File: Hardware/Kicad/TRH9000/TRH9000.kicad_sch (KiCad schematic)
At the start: 6 parts, among them J1 MSX_SLOT_CONNECTOR, U4 74HC138, U5 74HC32

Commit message: Footprint for the V9990
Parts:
- U4: footprint (none) -> Package_SO:SO-16_3.9x9.9mm_P1.27mm
- U5: footprint digikey-footprints:DIP-14_W3mm -> Package_SO:SO-14_3.9x8.65mm_P1.27mm
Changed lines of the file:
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@@
       (effects (font (size 1.27 1.27)) (justify left))
     )
-    (property "Footprint" "digikey-footprints:DIP-14_W3mm" (id 2) (at 165.1 120.65 0)
+    (property "Footprint" "Package_SO:SO-14_3.9x8.65mm_P1.27mm" (id 2) (at 165.1 120.65 0)
       (effects (font (size 1.524 1.524)) (justify left) hide)
     )
@@
       (effects (font (size 1.27 1.27)) (justify left))
     )
-    (property "Footprint" "" (id 2) (at 118.11 128.27 0)
+    (property "Footprint" "Package_SO:SO-16_3.9x9.9mm_P1.27mm" (id 2) (at 118.11 128.27 0)
       (effects (font (size 1.27 1.27)) hide)
     )
@@
     )
     (path "/d5c7e94e-ee8c-4fa2-b6f9-333fadc34caa/da6bfb64-a33a-4cf2-a14f-42ddd8c8c720"
-      (reference "C2") (unit 1) (value "100nF") (footprint "")
+      (reference "C2") (unit 1) (value "100nF") (footprint "Capacitor_SMD:C_0805_2012Metric")
     )
     (path "/d5c7e94e-ee8c-4fa2-b6f9-333fadc34caa/7abbb0b8-25fa-4ba9-afed-652280d66707"
@@
       (reference "R6") (unit 1) (value "4K7") (footprint "LED_SMD:LED_0805_2012Metric")
     )
-    (path "/d9ed34ef-ff83-4a70-a9f7-db0f42d1292e/67662d22-a245-4940-bd65-03651bcaa81c"
-      (reference "R7") (unit 1) (value "470R") (footprint "LED_SMD:LED_0805_2012Metric")
-    )
     (path "/d9ed34ef-ff83-4a70-a9f7-db0f42d1292e/bbaafd10-2e61-4d37-80f8-27fc5a2b4449"
       (reference "R8") (unit 1) (value "2K2") (footprint "LED_SMD:LED_0805_2012Metric")
     )
-    (path "/d9ed34ef-ff83-4a70-a9f7-db0f42d1292e/37410a4d-2046-4ddf-bb0e-18d481708b5d"
-      (reference "R9") (unit 1) (value "470R") (footprint "LED_SMD:LED_0805_2012Metric")
-    )
-    (path "/d9ed34ef-ff83-4a70-a9f7-db0f42d1292e/643d4177-75b8-41e9-8c82-b89d4a4fad42"
-      (reference "R10") (unit 1) (value "470R") (footprint "LED_SMD:LED_0805_2012Metric")
-    )
     (path "/d9ed34ef-ff83-4a70-a9f7-db0f42d1292e/fc1eeac4-dcc2-422b-a258-9423bfa5a1ef"
       (reference "R11") (unit 1) (value "4K7") (footprint "LED_SMD:LED_0805_2012Metric")
@@
       (reference "R23") (unit 1) (value "240R") (footprint "LED_SMD:LED_0805_2012Metric")
     )
+    (path "/d9ed34ef-ff83-4a70-a9f7-db0f42d1292e/ca541a19-f6cc-45bc-af9b-19d34164bfc7"
+      (reference "RV1") (unit 1) (value "500R") (footprint "Potentiometer_SMD:Potentiometer_Bourns_3314G_Vertical")
+    )
+    (path "/d9ed34ef-ff83-4a70-a9f7-db0f42d1292e/1325e162-b47f-49fb-8630-ad924a927842"
+      (reference "RV2") (unit 1) (value "500R") (footprint "Potentiometer_SMD:Potentiometer_Bourns_3314G_Vertical")
+    )
+    (path "/d9ed34ef-ff83-4a70-a9f7-db0f42d1292e/a3e1189c-b975-4c18-acc9-478a0dd0a5b4"
+      (reference "RV3") (unit 1) (value "500R") (footprint "Potentiometer_SMD:Potentiometer_Bourns_3314G_Vertical")
+    )
     (path "/d5c7e94e-ee8c-4fa2-b6f9-333fadc34caa/c04f413f-eb21-4d40-8e64-40127e6da87a"
-      (reference "U1") (unit 1) (value "V9990") (footprint "Ddraig:QFP-128_28x28_Pitch0.8mm")
+      (reference "U1") (unit 1) (value "V9990") (footprint "trh9000:QFP-128_28x28_Pitch0.8mm")
     )
     (path "/d5c7e94e-ee8c-4fa2-b6f9-333fadc34caa/957e464e-fa1e-4fdd-98f3-d28c0b05174e"
@@
     )
     (path "/f2de766b-6e04-4297-9ac6-8ed19da3519b"
-      (reference "U4") (unit 1) (value "74HC138") (footprint "")
+      (reference "U4") (unit 1) (value "74HC138") (footprint "Package_SO:SO-16_3.9x9.9mm_P1.27mm")
     )
     (path "/2c31a37b-5a2e-4dde-9eb0-70323652ba66"
-      (reference "U5") (unit 1) (value "74HC32") (footprint "digikey-footprints:DIP-14_W3mm")
+      (reference "U5") (unit 1) (value "74HC32") (footprint "Package_SO:SO-14_3.9x8.65mm_P1.27mm")
     )
     (path "/d9ed34ef-ff83-4a70-a9f7-db0f42d1292e/a944b42d-633e-4624-b6a6-e9241b129cf1"

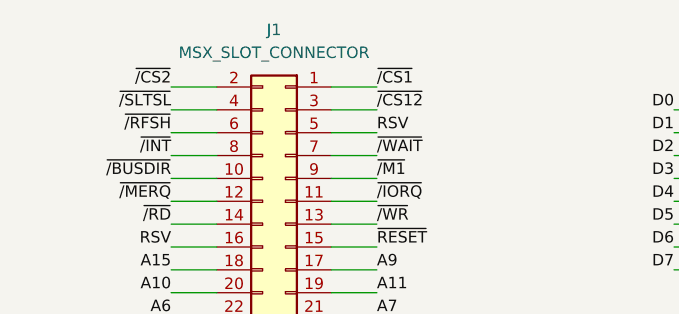
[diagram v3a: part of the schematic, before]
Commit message: Footprint adjusts
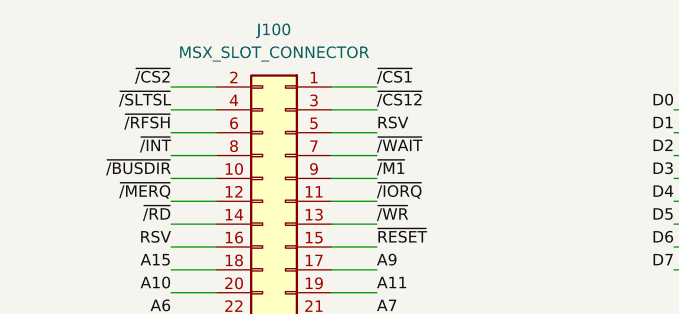
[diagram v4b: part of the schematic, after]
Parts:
- J100: renamed from J1; now left out of the parts list
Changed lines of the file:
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@@
   )
   (symbol (lib_id "Connector_Generic:Conn_02x25_Odd_Even") (at 48.26 55.88 0) (mirror y) (unit 1)
-    (in_bom yes) (on_board yes) (fields_autoplaced)
-    (property "Reference" "J1" (id 0) (at 46.99 19.05 0))
+    (in_bom no) (on_board yes) (fields_autoplaced)
+    (property "Reference" "J100" (id 0) (at 46.99 19.05 0))
     (property "Value" "MSX_SLOT_CONNECTOR" (id 1) (at 46.99 21.59 0))
     (property "Footprint" "msx:msx_cartridge" (id 2) (at 48.26 55.88 0)
@@
       (reference "C24") (unit 1) (value "220uF") (footprint "Capacitor_THT:CP_Radial_D5.0mm_P2.50mm")
     )
-    (path "/5c1dc888-6f7a-4cd6-bda7-5a87c57e6ccc"
-      (reference "J1") (unit 1) (value "MSX_SLOT_CONNECTOR") (footprint "msx:msx_cartridge")
+    (path "/d9ed34ef-ff83-4a70-a9f7-db0f42d1292e/c01ad78a-8b71-4615-ba6a-b588562a7eff"
+      (reference "J1") (unit 1) (value "RGB") (footprint "Connector_Dsub:DSUB-15-HD_Female_Horizontal_P2.29x1.98mm_EdgePinOffset3.03mm_Housed_MountingHolesOffset4.94mm")
     )
     (path "/d9ed34ef-ff83-4a70-a9f7-db0f42d1292e/8a9fe807-e426-499b-ab72-b66db1aca921"
@@
       (reference "J3") (unit 1) (value "Composite") (footprint "trh9000:KLPX0848A2RG")
     )
-    (path "/d9ed34ef-ff83-4a70-a9f7-db0f42d1292e/c01ad78a-8b71-4615-ba6a-b588562a7eff"
-      (reference "J4") (unit 1) (value "DB15_Female_HighDensity") (footprint "Connector_Dsub:DSUB-15-HD_Female_Horizontal_P2.29x1.98mm_EdgePinOffset3.03mm_Housed_MountingHolesOffset4.94mm")
+    (path "/5c1dc888-6f7a-4cd6-bda7-5a87c57e6ccc"
+      (reference "J100") (unit 1) (value "MSX_SLOT_CONNECTOR") (footprint "msx:msx_cartridge")
     )
     (path "/d5c7e94e-ee8c-4fa2-b6f9-333fadc34caa/ed13ecf5-0a7e-4a18-a92b-e7a01e79ff05"

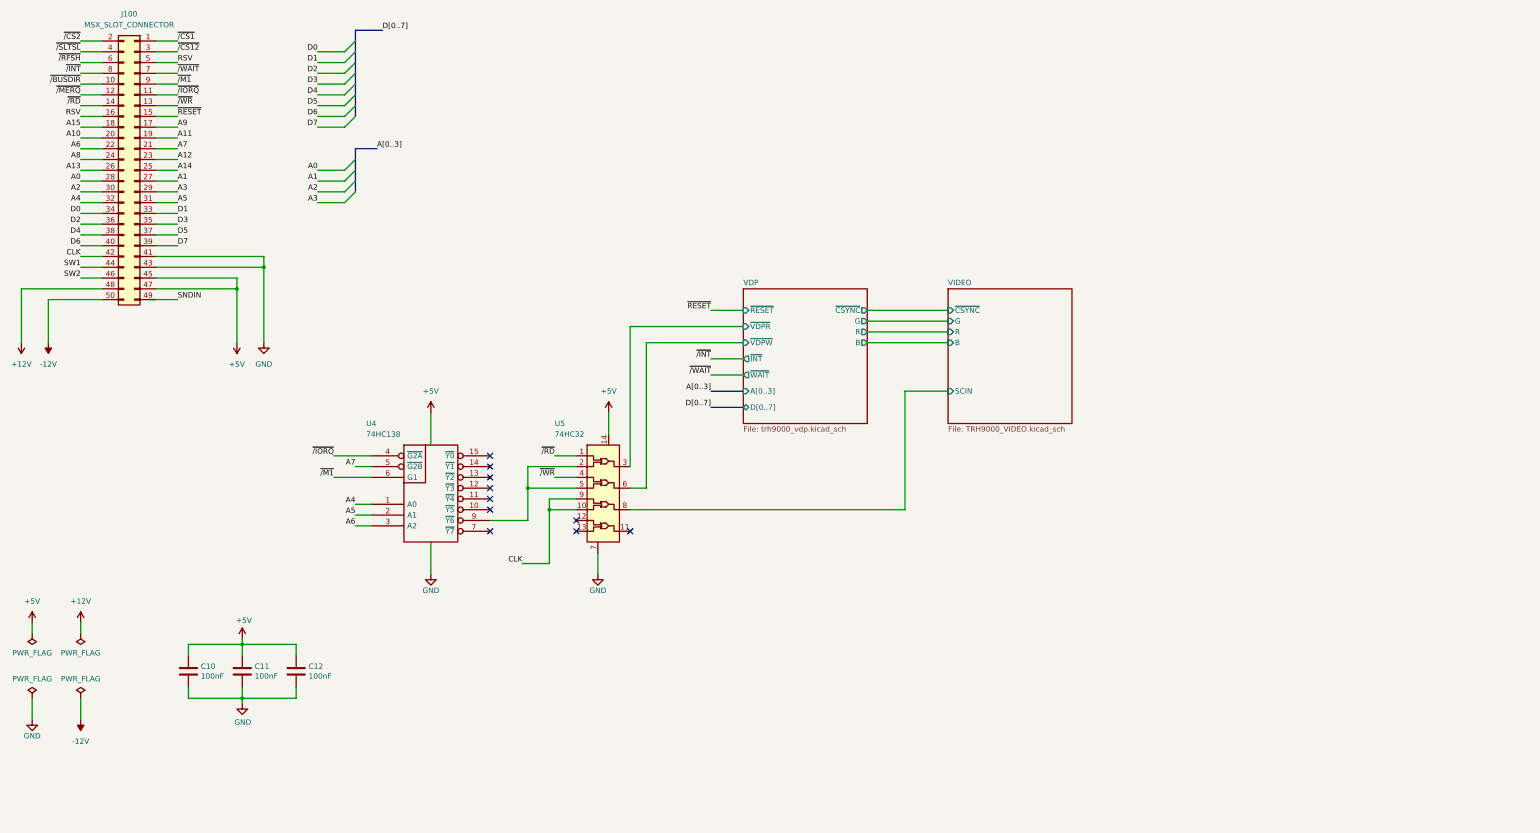
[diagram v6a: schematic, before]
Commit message: Many changes, among them, replacing the Composite out with SCART-rgb.
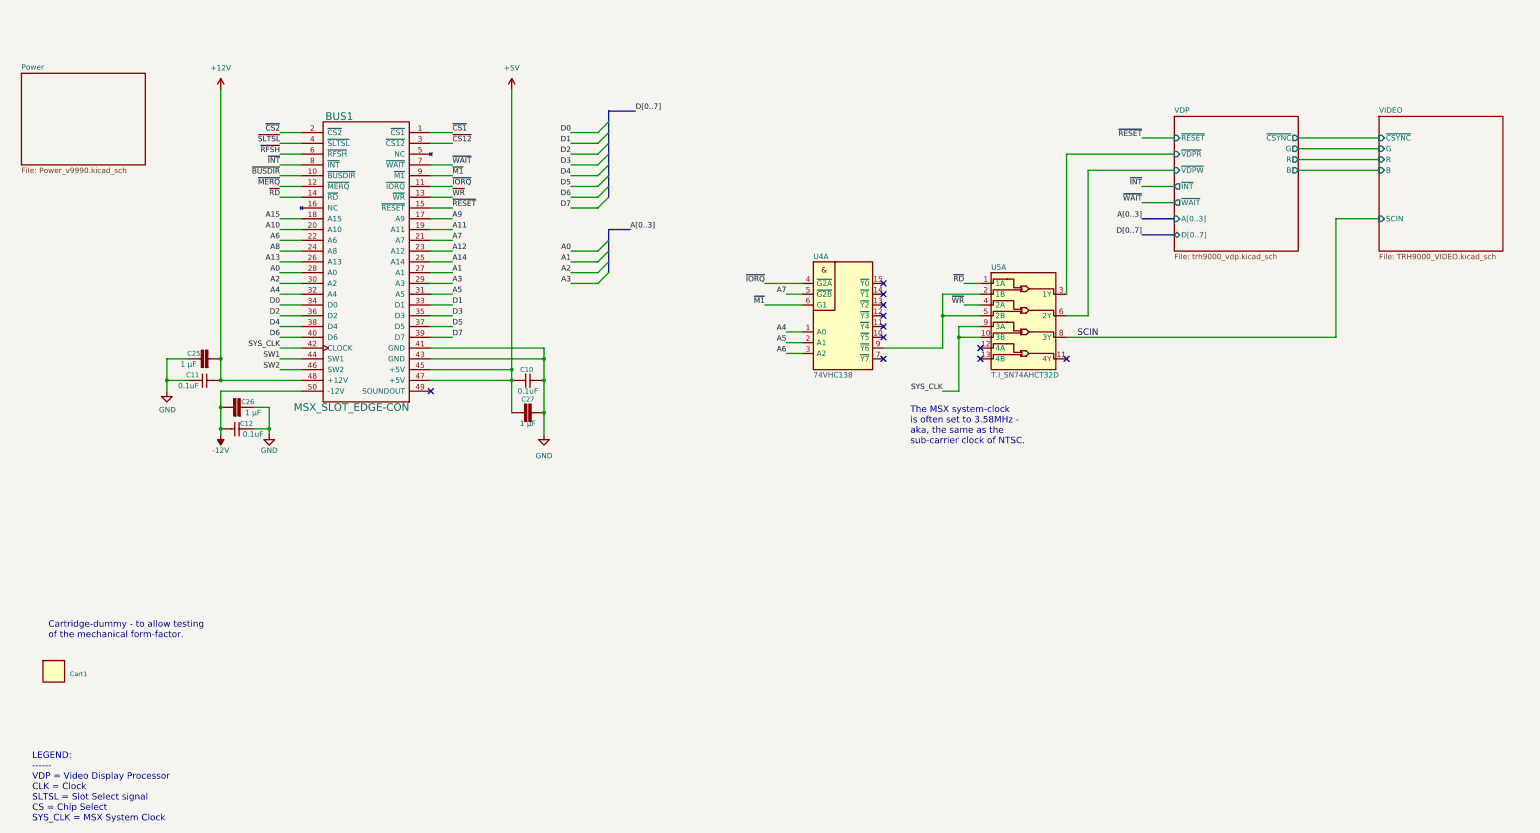
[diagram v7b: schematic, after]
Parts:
- removed C10, C11, C12: 100nF, Capacitor_SMD:C_0805_2012Metric, symbol Device:C
- removed J100: MSX_SLOT_CONNECTOR, msx:msx_cartridge, symbol Connector_Generic:Conn_02x25_Odd_Even
- added BUS1: MSX_SLOT_EDGE-CON, trh9000:msx_cartridge, symbol TRH9000:MSX_SLOT_EDGE-CON
- added C10, C11, C12: C_CC0805JPX7R9BB104, Capacitor_SMD:C_0805_2012Metric, symbol LRJ-parts:C_CC0805JPX7R9BB104
- added C25, C26, C27: C_CL21B105KBFNNNF, Capacitor_SMD:C_0805_2012Metric_Pad1.18x1.45mm_HandSolder, symbol LRJ-parts:C_CL21B105KBFNNNF
- added Cart1: MSX-cartridge_dummy, trh9000:MSX-cart-dummy, symbol TRH9000:MSX-cartridge_dummy
- U4: value 74HC138 -> 74VHC138; symbol 74xx_IEEE:74LS138 -> TRH9000:74VHC138; MPN (none) -> 74VHC138FT; Manufacturer (none) -> Toshiba Semiconductor and Storage
- U5: value 74HC32 -> T.I_SN74AHCT32D; footprint Package_SO:SO-14_3.9x8.65mm_P1.27mm -> trh9000:Texas_R-PDSO-G14_3.6x4.4mm; symbol dk_Logic-Gates-and-Inverters:SN74HC32N -> TRH9000:T.I_SN74AHCT32D; Category Integrated Circuits (ICs) -> (none); DK_Datasheet_Link http://www.ti.com/general/docs/suppproductinfo.tsp?distId=1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 -> (none); DK_Detail_Page /product-detail/en/texas-instruments/SN74HC32N/296-1589-5-N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 -> https://www.digikey.se/en/products/detail/texas-instruments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; Digi-Key_PN 296-1589-5-ND -> (none); Family Logic - Gates and Inverters -> (none); MPN SN74HC32N -> SN74AHCT32DGVR
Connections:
- net +12V: now also BUS1.48 (+12V), C11.2, C25.2
- net +5V: now also BUS1.45 (+5V), BUS1.47 (+5V), C10.1, C27.1; no longer U4.16 (VCC), U5.14 (VCC)
- net -12V: now also BUS1.50 (-12V), C12.1, C26.1
- net A0: now also BUS1.28 (A0)
- net A1: now also BUS1.27 (A1)
- net A10: now also BUS1.20 (A10)
- net A11: now also BUS1.19 (A11)
- net A12: now also BUS1.23 (A12)
- net A13: now also BUS1.26 (A13)
- net A14: now also BUS1.25 (A14)
- net A15: now also BUS1.18 (A15)
- net A2: now also BUS1.30 (A2)
- net A3: now also BUS1.29 (A3)
- net A4: now also BUS1.32 (A4)
- net A5: now also BUS1.31 (A5)
- net A6: now also BUS1.22 (A6)
- net A7: now also BUS1.21 (A7)
- net A8: now also BUS1.24 (A8)
- net A9: now also BUS1.17 (A9)
- net D0: now also BUS1.34 (D0)
- net D1: now also BUS1.33 (D1)
- net D2: now also BUS1.36 (D2~{})
- net D3: now also BUS1.35 (D3)
- net D4: now also BUS1.38 (D4)
- net D5: now also BUS1.37 (D5)
- net D6: now also BUS1.40 (D6)
- net D7: now also BUS1.39 (D7)
- net GND: now also BUS1.41 (GND), BUS1.43 (GND), C10.2, C11.1, C12.2, C25.1, C26.2, C27.2; no longer U4.8 (GND), U5.7 (GND)
- net SW1: now also BUS1.44 (SW1)
- net SW2: now also BUS1.46 (SW2)
- net ~{RESET}: now also BUS1.15 (~{RESET})
- net CLK renamed SYS_CLK
- net SYS_CLK: now also BUS1.42 (CLOCK)
- net VIDEO/SCIN renamed SCIN
- net ~{/IORQ} renamed ~{IORQ}
- net ~{IORQ}: now also BUS1.11 (~{IORQ})
- net ~{/M1} renamed ~{M1}
- net ~{M1}: now also BUS1.9 (~{M1})
- net ~{/RD} renamed ~{RD}
- net ~{RD}: now also BUS1.14 (~{RD})
- net ~{/WR} renamed ~{WR}
- net ~{WR}: now also BUS1.13 (~{WR})
- new net ~{BUSDIR}: BUS1.10 (~{BUSDIR})
- new net ~{CS12}: BUS1.3 (~{CS12})
- new net ~{CS1}: BUS1.1 (~{CS1})
- new net ~{CS2}: BUS1.2 (~{CS2})
- new net ~{INT}: BUS1.8 (~{INT})
- new net ~{MERQ}: BUS1.12 (~{MERQ})
- new net ~{RFSH}: BUS1.6 (~{RFSH})
- new net ~{SLTSL}: BUS1.4 (~{SLTSL})
- new net ~{WAIT}: BUS1.7 (~{WAIT})
- no-connect marks 10 -> 11
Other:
- added sheet Power (Power_v9990.kicad_sch)
- note added: "Cartridge-dummy - to allow testing of the mechanical form-factor."
- note added: "LEGEND: ------ VDP = Video Display Processor CLK = Clock SLTSL = Slot Select signal CS = Chip Select SYS_CLK = MSX System Clock"
- note added: "The MSX system-clock is often set to 3.58MHz - aka, the same as the sub-carrier clock of NTSC."

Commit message: Multiple updates. Routing. Almost finished routing for the VDP. Moved back the footprint for the 14mhz oscillator to THT as it is easier to find outside US/Europe and I have a bunch laying around here. Organized all components into the PCB. Removed the holed in the cartridge so I can better measure them in the standard MSX cartridge. Changed the RGB connector footprint to a shorter version so we can fit it in the standard size cartridge. Fixed multiple footprints to 0805 as we will be standardizing in that size.
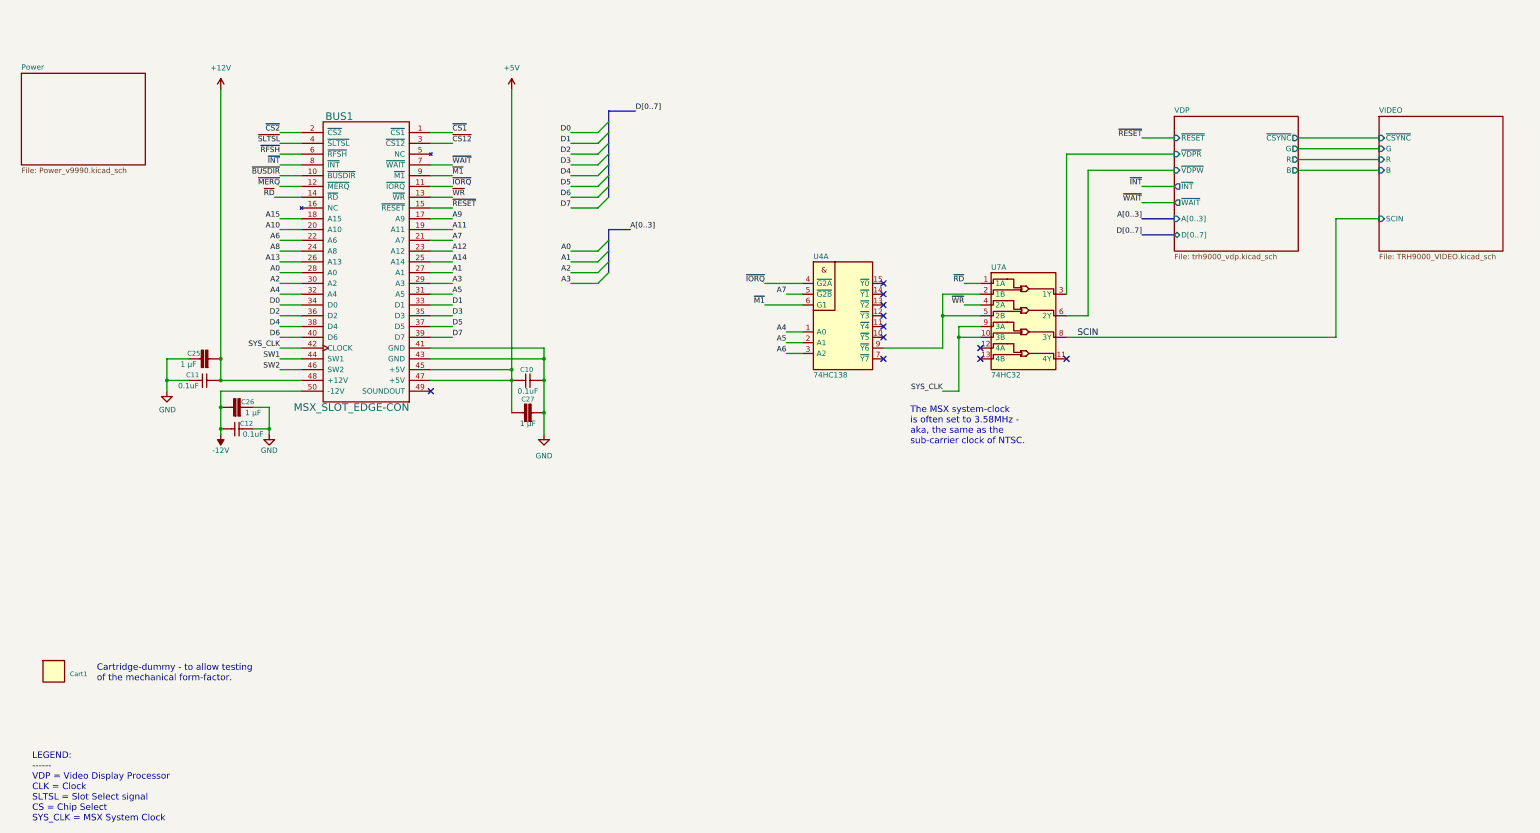
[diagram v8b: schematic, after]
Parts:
- C10: value C_CC0805JPX7R9BB104 -> 0.1uF; MPN CC0805JPX7R9BB104 -> (none); Manufacturer Yageo -> (none); Mouser datasheet https://www.mouser.se/datasheet/2/427/vjcommercialseries-17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 -> (none)
- C11, C12: value C_CC0805JPX7R9BB104 -> 0.1uF
- C25, C26, C27: value C_CL21B105KBFNNNF -> 1 µF; footprint Capacitor_SMD:C_0805_2012Metric_Pad1.18x1.45mm_HandSolder -> Capacitor_SMD:C_0805_2012Metric
- U4: value 74VHC138 -> 74HC138; MPN 74VHC138FT -> 74HC138
- U7: renamed from U5; value T.I_SN74AHCT32D -> 74HC32; footprint trh9000:Texas_R-PDSO-G14_3.6x4.4mm -> Package_SO:SO-14_3.9x8.65mm_P1.27mm; MPN SN74AHCT32DGVR -> 74HC32
